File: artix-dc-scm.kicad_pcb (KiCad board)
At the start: 8 copper layers, 90 x 120.4 mm, 428 parts, among them IC1 TPS54561, J12 S2B-PH-K-S_LF__SN_, J13 62000311121, J2 1-2199230-6, J3 543630489, J4 M20-7830642, J5 SFF-TA-1002-4C+, J6 0878311420, J7 61300611121, Q1 IRLML6402TRPBF, Q10 2N7002, Q11 2N7002, Q12 2N7002, Q13 2N7002, Q14 2N7002, Q15 2N7002, Q16 2N7002, Q2 IRLML6402TRPBF, Q3 IRLML6402TRPBF, Q4 IRLML6402TRPBF, Q5 IRLML6402TRPBF, Q6 IRLML6402TRPBF, Q7 2N7002, Q8 2N7002, Q9 2N7002, U1 DP83848JSQ_NOPB, U10 TPS62823DLCT, U11 TPS62823DLCT, U12 TPS62823DLCT, U13 TPS62823DLCT, U14 XC7A100T-FGG484, U15 SN74LVC1G08DCKR, U16 SN74LS08DBR, U17 EMMC04G-S100-B08U, U18 MAX3421EEHJ, U19 FT245RQ, U2 W25Q32JVSSIQ_TR, U3 W25Q32JVSSIQ_TR, U4 W25Q32JVSSIQ_TR, U5 W25Q32JVSSIQ_TR, U6 NVT2008DQ,115, U7 AS4C256M16D3, U8 TPS51200DRC, U9 LM3881MME_NOPB, Y1 ABM8G-12.000MHZ-18-D2Y-T, Y2 ABM8G-25.000MHZ-18-D2Y-T

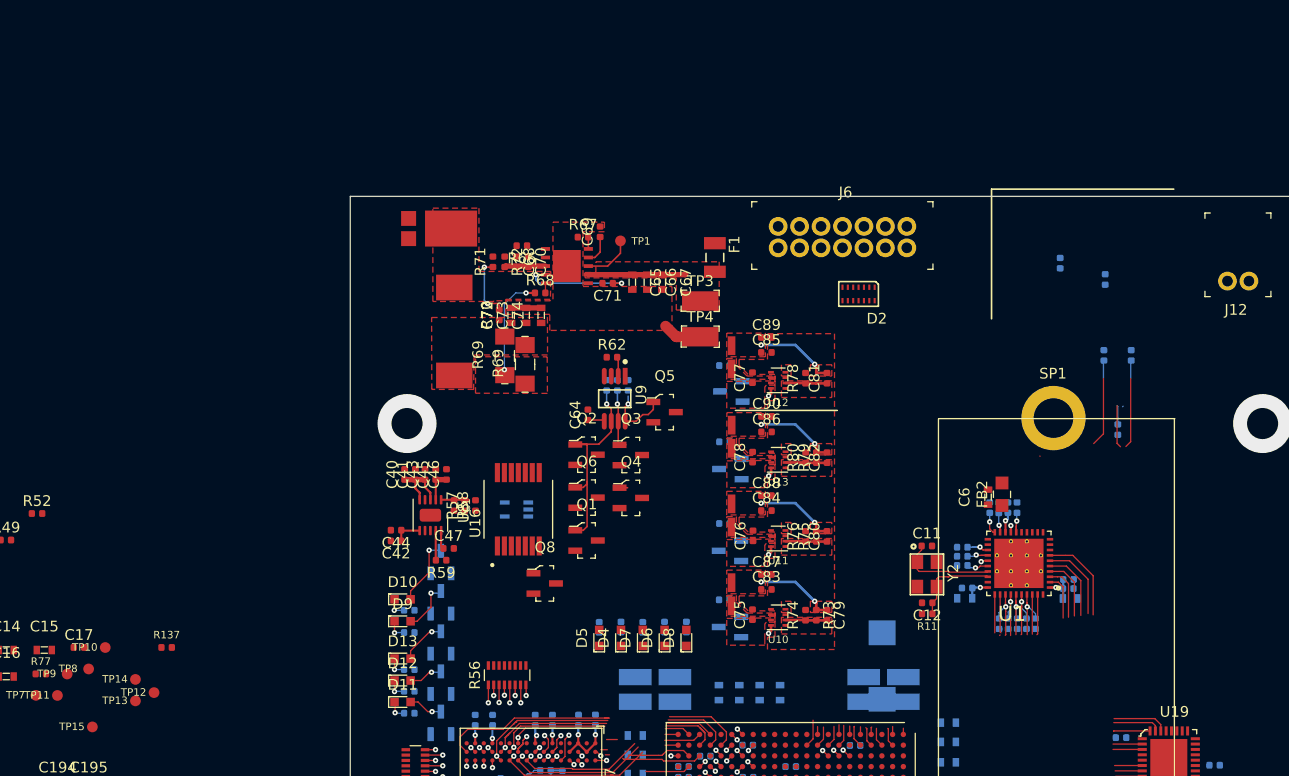
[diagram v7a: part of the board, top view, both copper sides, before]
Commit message: Change M.2 description in README
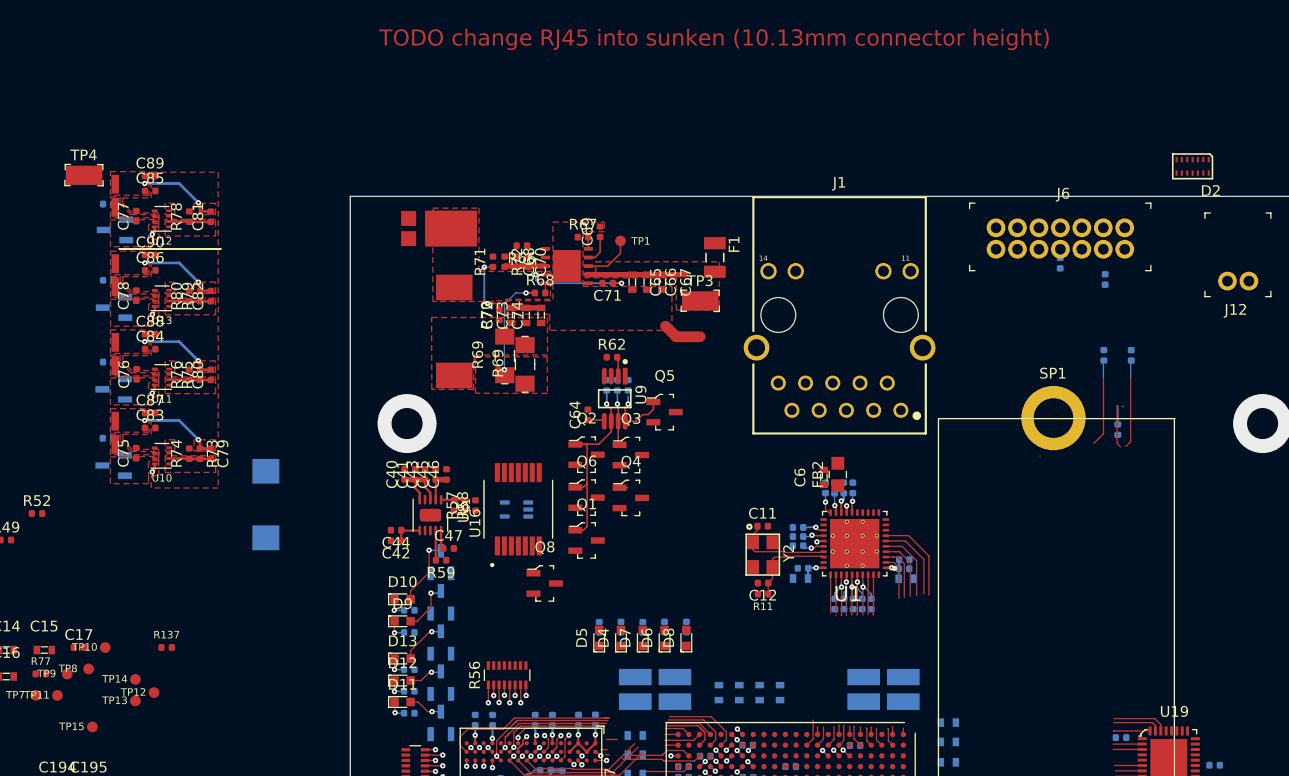
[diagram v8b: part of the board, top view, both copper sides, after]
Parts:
- added J1: WE-RJ45_7499111121A, artix-dc-scm-footprints:7499111121A, F.Cu at (105.7, 70.0)
- moved C150 59.4 mm to (52.2, 87.6)
- moved C75 59.4 mm to (40.1, 82.8)
- moved C77 59.4 mm to (40.1, 60.7)
- moved C79 59.4 mm to (47.1, 82.9)
- moved C80 59.4 mm to (47.1, 75.5)
- moved C81 59.4 mm to (47.1, 60.8)
- moved C86 59.4 mm to (41.4, 65.8)
- moved C90 59.4 mm to (41.4, 64.4)
- moved L5 59.4 mm to (38.2, 66.3)
- moved Q11 59.4 mm to (38.0, 84.0)
- moved Q9 59.4 mm to (38.0, 76.9)
- moved R73 59.4 mm to (46.1, 82.9)
- moved R74 59.4 mm to (45.1, 82.9)
- moved R75 59.4 mm to (46.1, 75.5)
- moved R76 59.4 mm to (45.1, 75.5)
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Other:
- board text added: "TODO change RJ45 into sunken (10.13mm connector height)"
